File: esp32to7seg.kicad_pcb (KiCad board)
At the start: 2 copper layers, 60 x 90 mm, 88 parts, among them J1 Conn_01x05, J2 Barrel_Jack_Switch, J3 Conn_01x03, J4 Conn_01x04_Pin, J5 Conn_01x04_Pin, J6 Conn_01x04_Pin, J7 Conn_01x04_Pin, Q1 BC848, Q10 BC807, Q11 BC817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

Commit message: Route this stuff...
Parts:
- moved C8 107.1 mm to (166.8, 125.4)
- moved C7 75.8 mm to (189.0, 116.4), turned to -90 degrees
- moved Q16 75.6 mm to (174.0, 97.1), turned to 90 degrees
- moved C6 75.0 mm to (187.0, 110.4)
- moved R1 74.0 mm to (172.2, 51.4), turned to -90 degrees
- moved Q18 73.7 mm to (170.5, 97.1), turned to -90 degrees
- moved R2 71.2 mm to (169.4, 54.4)
- moved R39 67.4 mm to (174.0, 100.1), turned to 180 degrees
- moved R11 66.5 mm to (188.8, 123.4), turned to 90 degrees
- moved Q12 65.2 mm to (174.2, 86.1), turned to 90 degrees
- moved R42 64.9 mm to (170.5, 94.1)
- moved Q14 64.3 mm to (170.6, 86.1), turned to -90 degrees
- moved Q15 62.5 mm to (186.0, 86.8), turned to 90 degrees
- moved R4 62.4 mm to (155.8, 101.2), turned to 90 degrees
- moved R43 60.8 mm to (174.0, 94.1)
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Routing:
- net GND: track 25.1 -> 369.9 mm, vias 1 -> 18
- net +9V: track 11.8 -> 163.1 mm, vias 0 -> 6
- net +3V3: track 3.28 -> 152.8 mm, vias 0 -> 2
- net Net-(J5-Pin_4): track 0.00 -> 82.0 mm, vias 0 -> 1
- net /BOOT_SEL: track 0.00 -> 74.0 mm
- net Net-(J5-Pin_3): track 0.00 -> 71.8 mm, vias 0 -> 1
- net /EN: track 0.00 -> 64.9 mm
- net /Led Driver/CLK: track 0.00 -> 63.9 mm, vias 0 -> 2
- net Net-(J5-Pin_2): track 0.00 -> 61.4 mm, vias 0 -> 1
- net /Led Driver/DIN: track 0.00 -> 61.3 mm, vias 0 -> 2
- net /Led Driver/SEG_A: track 0.00 -> 61.3 mm
- net /Led Driver/~{CS}: track 0.00 -> 57.5 mm, vias 0 -> 2
- net Net-(J4-Pin_1): track 0.00 -> 56.2 mm, vias 0 -> 1
- net Net-(J5-Pin_1): track 0.00 -> 51.5 mm, vias 0 -> 1
- net /Led Driver/SEG_B: track 0.00 -> 49.8 mm
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- added copper zone on F.Cu, net +3V3
- added copper zone on B.Cu, net +9V
- added copper zone on F.Cu, net +9V
- added copper zone on B.Cu, net GND
- added copper zone on F.Cu, net GND
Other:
- board text added: "G TX RX DTR RTS"
- board text added: "M.G. 10/23"

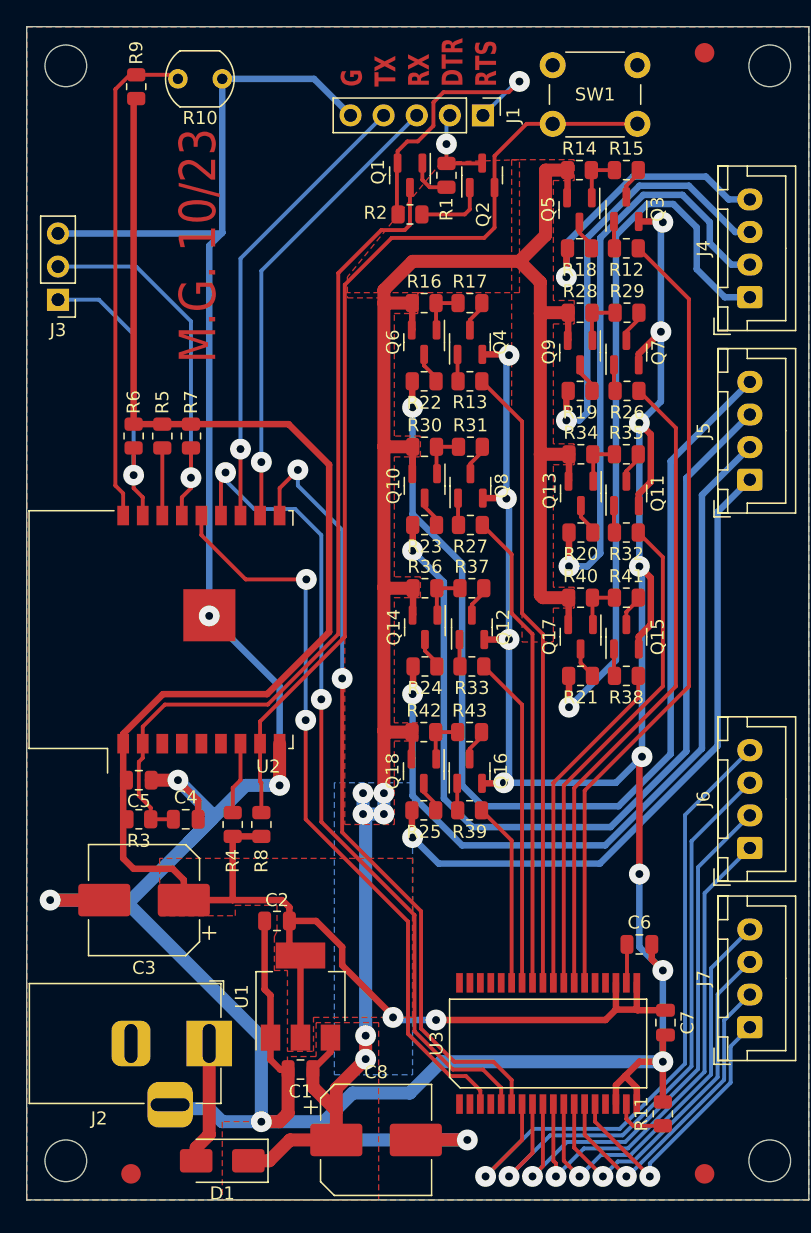
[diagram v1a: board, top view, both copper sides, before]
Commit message: Fix DRC violations.
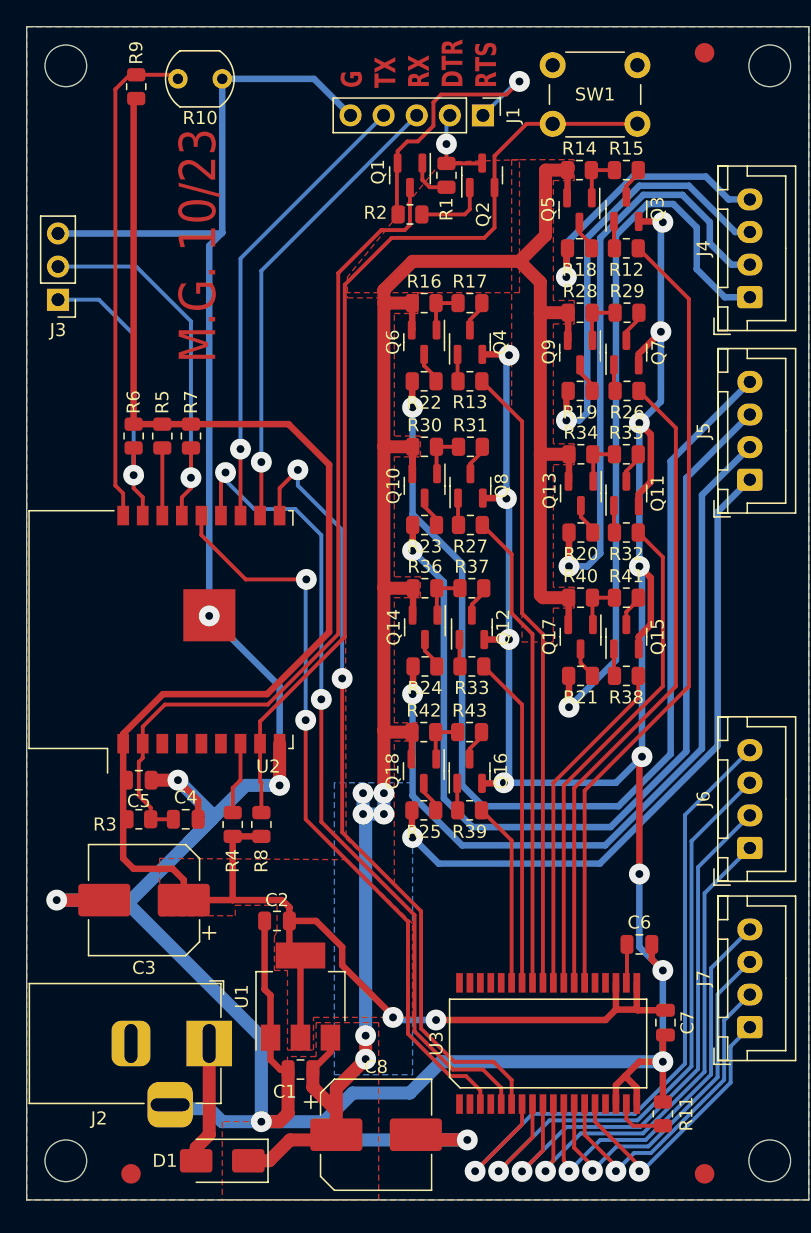
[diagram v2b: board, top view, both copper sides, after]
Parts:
- moved C8 0.40 mm to (166.8, 125.0)
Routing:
- net GND: track 369.9 -> 369.1 mm
- net /Led Driver/DIG7: track 21.9 -> 21.2 mm
- net /Led Driver/DIG2: track 43.1 -> 43.7 mm
- net /Led Driver/DIG0: track 51.7 -> 52.3 mm
- net /Led Driver/DIG1: track 47.4 -> 48.0 mm
- net /Led Driver/DIG3: track 39.0 -> 39.5 mm

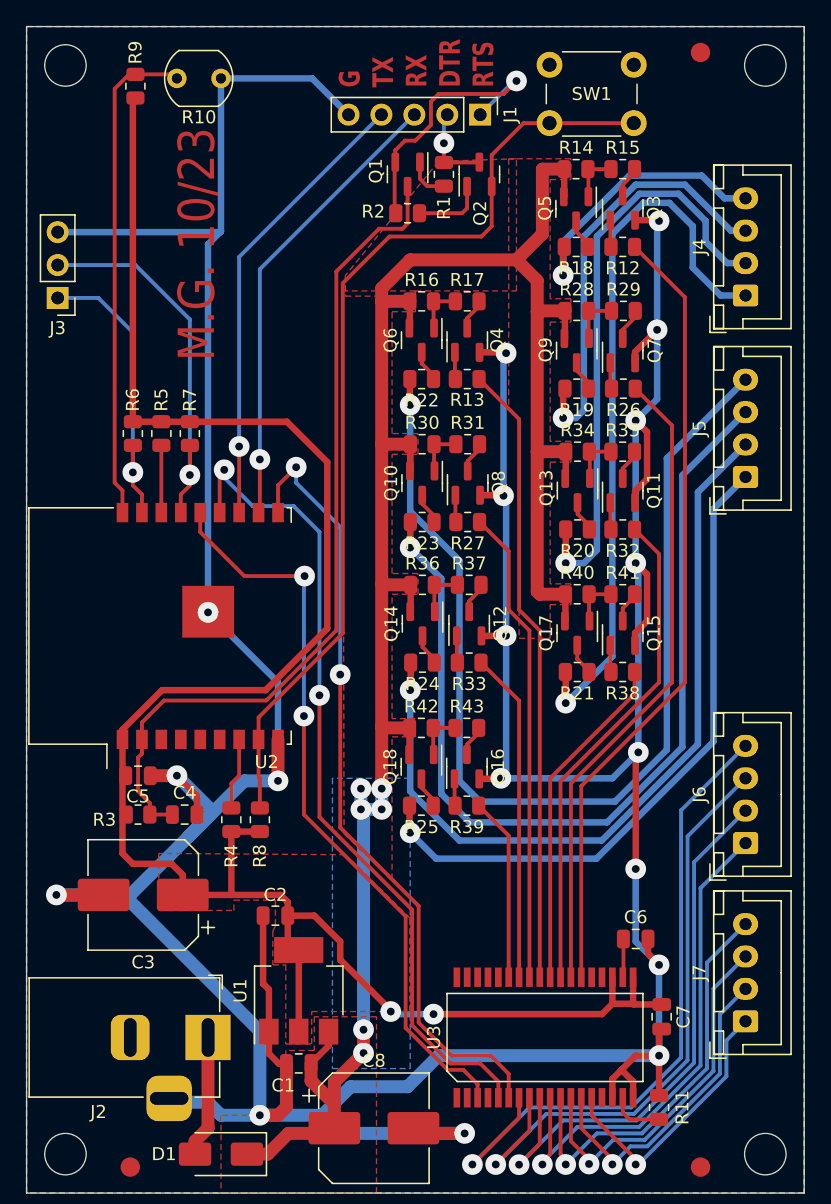
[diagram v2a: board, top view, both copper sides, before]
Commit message: Add 3v3 pin to i2c header.
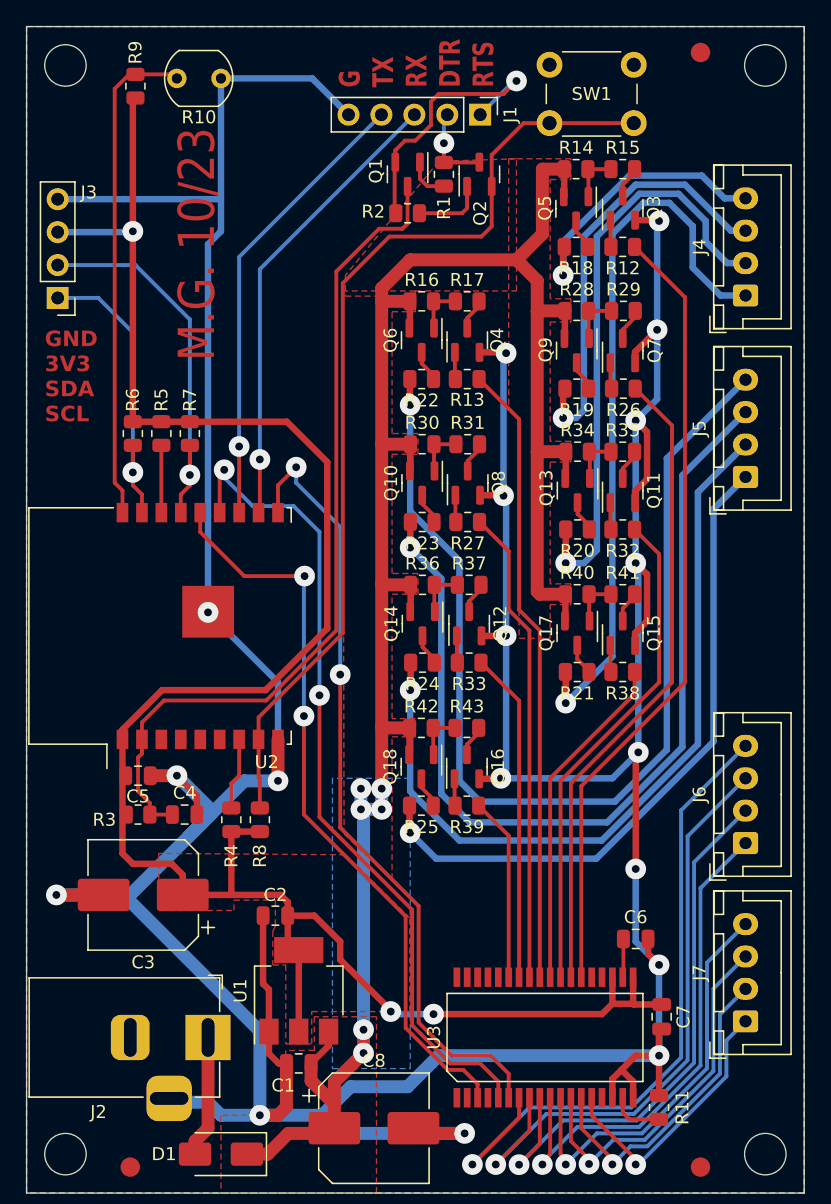
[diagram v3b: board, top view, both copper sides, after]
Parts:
- J3: value Conn_01x03 -> Conn_01x04; footprint Connector_PinHeader_2.54mm:PinHeader_1x03_P2.54mm_Vertical -> Connector_PinHeader_2.54mm:PinHeader_1x04_P2.54mm_Vertical
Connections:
- J3 pad 3: GND -> +3V3
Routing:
- net +3V3: track 152.8 -> 158.6 mm, vias 2 -> 3
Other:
- board text added: "GND 3V3 SDA SCL"

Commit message: Multiple improvements
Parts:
- removed Q1, Q2: BC848, Package_TO_SOT_SMD:SOT-23
- removed R1, R2: 10k, Resistor_SMD:R_0805_2012Metric
- added R44: 10k, Resistor_SMD:R_0805_2012Metric, F.Cu at (159.5, 73.5)
- added SW2: SW_Push, Button_Switch_THT:SW_PUSH_6mm, F.Cu at (163.0, 43.0)
- J1: value Conn_01x05 -> Conn_01x04_Pin; footprint Connector_PinHeader_2.54mm:PinHeader_1x05_P2.54mm_Vertical -> Connector_PinHeader_2.54mm:PinHeader_1x04_P2.54mm_Vertical
- moved J1 29.7 mm to (156.5, 70.0), turned to 180 degrees
- moved R4 1.20 mm to (157.0, 101.2)
- moved R8 1.00 mm to (159.0, 101.2)
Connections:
- J1 pad 1: /RTS -> unconnected-(J1-Pin_1-Pad1)
- J1 pad 2: /DTR -> /USB+
- J1 pad 3: /RXD -> /USB-
- J1 pad 4: /TXD -> GND
- U2 pad 10: /Led Driver/DIN -> /BUTTON2
- U2 pad 11: /RXD -> unconnected-(U2-RXD-Pad11)
- U2 pad 12: /TXD -> unconnected-(U2-TXD-Pad12)
- U2 pad 13: /Led Driver/CLK -> /USB-
- U2 pad 14: /Led Driver/~{CS} -> /USB+
- U2 pad 4: unconnected-(U2-IO5-Pad4) -> /Led Driver/~{CS}
- U2 pad 5: unconnected-(U2-IO6-Pad5) -> /Led Driver/CLK
- U2 pad 6: unconnected-(U2-IO7-Pad6) -> /Led Driver/DIN
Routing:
- net /EN: track 64.9 -> 8.04 mm
- net /BUTTON2: track 0.00 -> 42.7 mm, vias 0 -> 3
- net /RXD: track 35.7 -> 0.00 mm, vias 1 -> 0
- net /TXD: track 35.2 -> 0.00 mm, vias 1 -> 0
- net GND: track 369.1 -> 398.4 mm
- net /Led Driver/CLK: track 63.9 -> 42.0 mm
- net /RTS: track 21.4 -> 0.00 mm, vias 1 -> 0
- net /Led Driver/DIN: track 61.3 -> 42.0 mm
- net /Led Driver/~{CS}: track 57.5 -> 41.7 mm
- net /USB-: track 0.00 -> 14.9 mm, vias 0 -> 1
- net /USB+: track 0.00 -> 11.3 mm, vias 0 -> 1
- net /DTR: track 6.54 -> 0.00 mm, vias 1 -> 0
- net Net-(Q2-B): track 5.51 -> 0.00 mm
- net Net-(Q1-B): track 3.37 -> 0.00 mm
- net /BOOT_SEL: track 74.0 -> 71.6 mm, vias 0 -> 1
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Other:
- board text added: "GND D- D+"
- board text added: "M.G. 01/25"
- board text removed: "G TX RX DTR RTS"
- board text removed: "M.G. 10/23"
